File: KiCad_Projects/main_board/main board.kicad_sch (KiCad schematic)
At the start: 69 parts

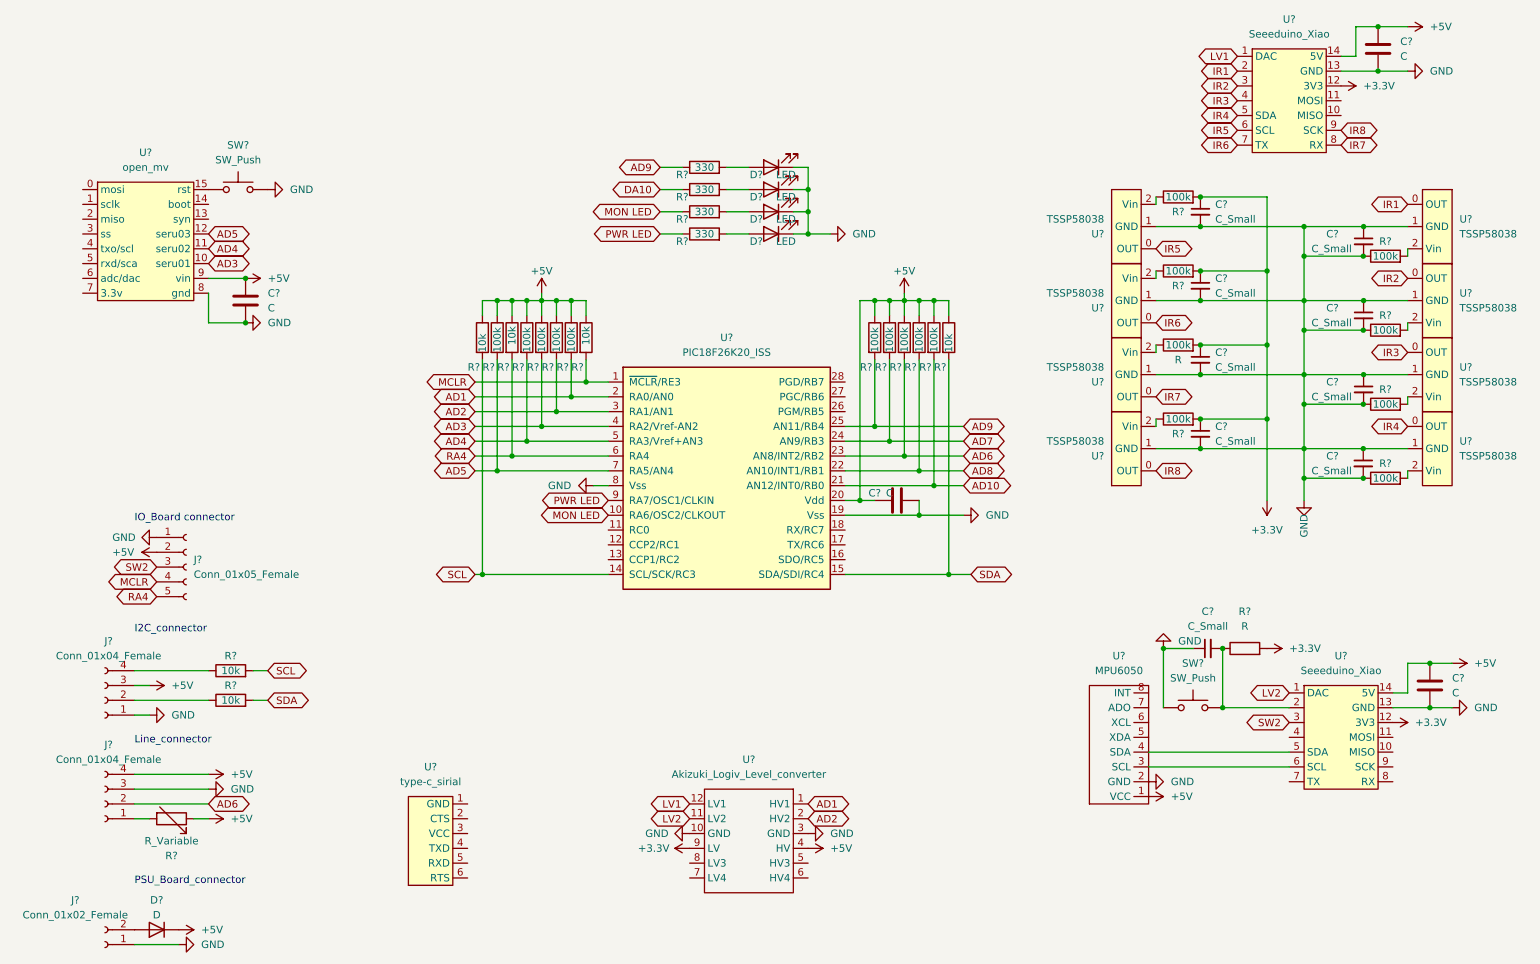
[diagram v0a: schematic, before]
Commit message: 基板データの更新
IO基板、ライン基板、電源基盤のコネクタ変更、最終確認
メイン基板制作中。
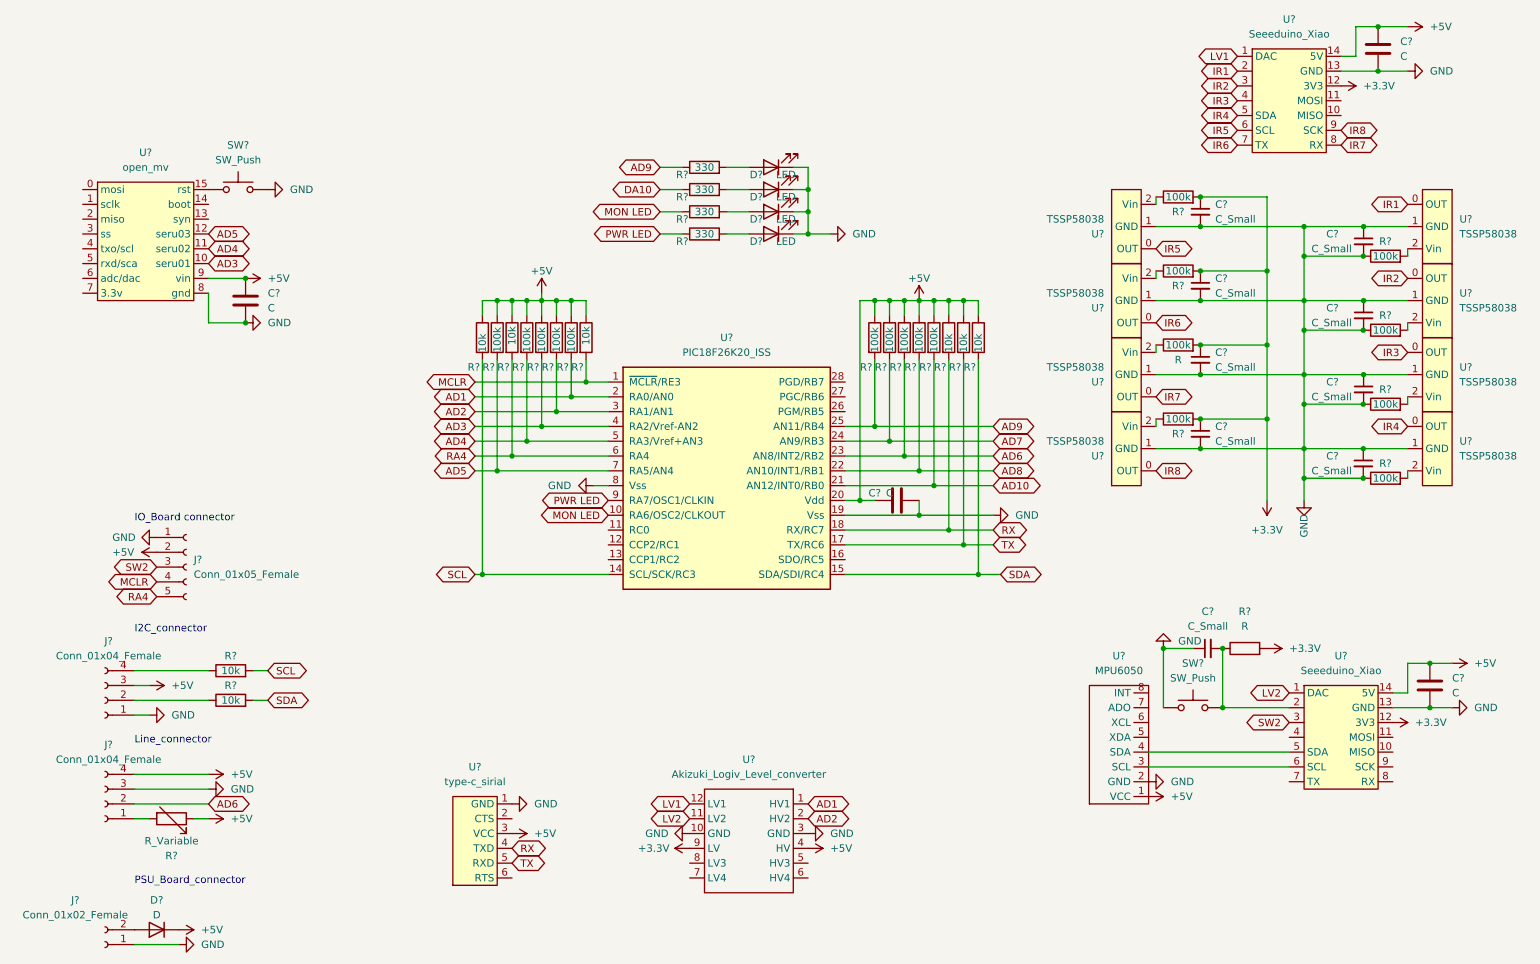
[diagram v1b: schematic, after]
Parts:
- added R? (x2): 10k, symbol Device:R
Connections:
- net +5V: now also U?.3 (VCC), R?.1, R?.1
- net GND: now also U?.1 (GND)
- net SDA: now also R?.2; no longer R?.2
- net RX: now reaches U?.4 (TXD)
- net RX: now also R?.2, U?.18 (RX/RC7)
- net TX: now reaches U?.5 (RXD)
- net TX: now also U?.17 (TX/RC6), R?.2
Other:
- moved on the sheet: U?
